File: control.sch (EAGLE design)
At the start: 71 parts, among them IC2 XMEGA16A4A, IC3 LM317MBSTT3, IC5 LM358N, Q1 BSS123, Q2 BSS123, Q3 BC548, Q4 BC557C, Q5 TIP41C, Q6 TIP42C, Q7 BC338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

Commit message: adc angeschlossen
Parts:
- removed JP4, JP6: (no value), jumper:JP4E
- renumbered R17 to R7
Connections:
- new net N$10: R44.2
- new net N$38: R47.2
- new net N$39: R48.2
- new net N$5: R43.2
- net ADC1: now also R45.2
- net ADC2: now also R46.2
- net ADC3: now also R42.2
- net ADC4: now also R41.2, R7.2; no longer R7.1
- net DIS_A: now also IC2.PE3; no longer IC2.PD0
- net EN_A1: now also IC2.PE2; no longer IC2.PD1
- net N$16: now also R7.1; no longer R7.2
- net N$18: no longer JP6.4
- net N$19: no longer JP6.3
- net N$20: no longer JP6.2
- net N$21: no longer JP6.1
- net N$22: no longer JP4.4
- net N$23: no longer JP4.3
- net N$24: no longer JP4.2
- net N$25: no longer JP4.1
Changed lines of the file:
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@@
 <part name="U$3" library="teile" deviceset="STL100NH3LL" device=""/>
 <part name="R16" library="resistor-power" deviceset="R" device="KH208-8R" value="4R7"/>
-<part name="R17" library="resistor-power" deviceset="R" device="KH208-8R" value="4R7"/>
 <part name="IC2" library="atmel" deviceset="XMEGA16A4" device="A"/>
 <part name="C1" library="resistor" deviceset="C-EU" device="C0805K"/>
@@
 <part name="+3V4" library="supply1" deviceset="+3V3" device=""/>
 <part name="P+3" library="supply1" deviceset="+12V" device=""/>
-<part name="JP4" library="jumper" deviceset="JP4E" device=""/>
-<part name="JP6" library="jumper" deviceset="JP4E" device=""/>
 <part name="R13" library="resistor" deviceset="R-EU_" device="M0805"/>
 <part name="R21" library="resistor" deviceset="R-EU_" device="M0805"/>
@@
 <part name="+3V5" library="supply1" deviceset="+3V3" device=""/>
 <part name="GND14" library="supply1" deviceset="GND" device=""/>
+<part name="R7" library="resistor-power" deviceset="R" device="KH208-8R" value="4R7"/>
 </parts>
 <sheets>
@@
 <instance part="U$3" gate="G$1" x="22.86" y="33.02"/>
 <instance part="R16" gate="G$1" x="30.48" y="48.26" rot="R90"/>
-<instance part="R17" gate="G$1" x="30.48" y="73.66" rot="R270"/>
 <instance part="IC2" gate="G$1" x="129.54" y="198.12"/>
 <instance part="C1" gate="G$1" x="91.44" y="210.82"/>
@@
 <instance part="+3V4" gate="G$1" x="60.96" y="266.7"/>
 <instance part="P+3" gate="1" x="25.4" y="266.7"/>
-<instance part="JP4" gate="G$1" x="213.36" y="233.68" rot="R270"/>
-<instance part="JP6" gate="G$1" x="213.36" y="223.52" rot="R270"/>
 <instance part="R13" gate="G$1" x="7.62" y="137.16" rot="R270"/>
 <instance part="R21" gate="G$1" x="45.72" y="119.38" rot="R270"/>
@@
 <instance part="+3V5" gate="G$1" x="71.12" y="233.68"/>
 <instance part="GND14" gate="1" x="76.2" y="233.68"/>
+<instance part="R7" gate="G$1" x="30.48" y="73.66" rot="R90"/>
 </instances>
 <busses>
@@
 <pinref part="IC5" gate="A" pin="-IN"/>
 <wire x1="147.32" y1="60.96" x2="144.78" y2="60.96" width="0.1524" layer="91"/>
+</segment>
+<segment>
+<pinref part="R46" gate="G$1" pin="2"/>
+<wire x1="198.12" y1="256.54" x2="198.12" y2="248.92" width="0.1524" layer="91"/>
+<label x="198.12" y="251.46" size="1.778" layer="95" rot="R90"/>
 </segment>
 </net>
@@
 <junction x="50.8" y="76.2"/>
 </segment>
+<segment>
+<pinref part="R45" gate="G$1" pin="2"/>
+<wire x1="195.58" y1="248.92" x2="195.58" y2="256.54" width="0.1524" layer="91"/>
+<label x="195.58" y="251.46" size="1.778" layer="95" rot="R90"/>
+</segment>
 </net>
 <net name="N$4" class="0">
@@
 <wire x1="96.52" y1="58.42" x2="91.44" y2="58.42" width="0.1524" layer="91"/>
 <junction x="91.44" y="58.42"/>
+</segment>
+<segment>
+<pinref part="R42" gate="G$1" pin="2"/>
+<wire x1="187.96" y1="256.54" x2="187.96" y2="248.92" width="0.1524" layer="91"/>
+<label x="187.96" y="251.46" size="1.778" layer="95" rot="R90"/>
 </segment>
 </net>
@@
 <pinref part="JP5" gate="G$1" pin="2"/>
 <wire x1="25.4" y1="58.42" x2="30.48" y2="58.42" width="0.1524" layer="91"/>
-<pinref part="R17" gate="G$1" pin="2"/>
 <wire x1="30.48" y1="58.42" x2="30.48" y2="68.58" width="0.1524" layer="91"/>
+<pinref part="R7" gate="G$1" pin="1"/>
 </segment>
 </net>
@@
 <wire x1="30.48" y1="81.28" x2="30.48" y2="99.06" width="0.1524" layer="91"/>
 <wire x1="30.48" y1="99.06" x2="45.72" y2="99.06" width="0.1524" layer="91"/>
-<pinref part="R17" gate="G$1" pin="1"/>
 <wire x1="30.48" y1="78.74" x2="30.48" y2="81.28" width="0.1524" layer="91"/>
 <junction x="30.48" y="81.28"/>
@@
 <wire x1="55.88" y1="137.16" x2="55.88" y2="132.08" width="0.1524" layer="91"/>
 <junction x="63.5" y="137.16"/>
+<pinref part="R7" gate="G$1" pin="2"/>
+</segment>
+<segment>
+<pinref part="R41" gate="G$1" pin="2"/>
+<wire x1="185.42" y1="248.92" x2="185.42" y2="256.54" width="0.1524" layer="91"/>
+<label x="185.42" y="251.46" size="1.778" layer="95" rot="R90"/>
 </segment>
 </net>
@@
 <pinref part="IC2" gate="G$1" pin="PA0"/>
 <wire x1="157.48" y1="218.44" x2="185.42" y2="218.44" width="0.1524" layer="91"/>
-<pinref part="JP6" gate="G$1" pin="4"/>
 <pinref part="R33" gate="G$1" pin="2"/>
 <wire x1="185.42" y1="218.44" x2="210.82" y2="218.44" width="0.1524" layer="91"/>
@@
 <pinref part="IC2" gate="G$1" pin="PA1"/>
 <wire x1="157.48" y1="220.98" x2="187.96" y2="220.98" width="0.1524" layer="91"/>
-<pinref part="JP6" gate="G$1" pin="3"/>
 <pinref part="R42" gate="G$1" pin="1"/>
 <pinref part="R34" gate="G$1" pin="2"/>
@@
 <pinref part="IC2" gate="G$1" pin="PA2"/>
 <wire x1="157.48" y1="223.52" x2="190.5" y2="223.52" width="0.1524" layer="91"/>
-<pinref part="JP6" gate="G$1" pin="2"/>
 <pinref part="R35" gate="G$1" pin="2"/>
 <pinref part="R43" gate="G$1" pin="1"/>
@@
 <pinref part="IC2" gate="G$1" pin="PA3"/>
 <wire x1="210.82" y1="226.06" x2="193.04" y2="226.06" width="0.1524" layer="91"/>
-<pinref part="JP6" gate="G$1" pin="1"/>
 <pinref part="R44" gate="G$1" pin="1"/>
 <pinref part="R36" gate="G$1" pin="2"/>
@@
 <pinref part="IC2" gate="G$1" pin="PA4"/>
 <wire x1="157.48" y1="228.6" x2="195.58" y2="228.6" width="0.1524" layer="91"/>
-<pinref part="JP4" gate="G$1" pin="4"/>
 <pinref part="R37" gate="G$1" pin="2"/>
 <pinref part="R45" gate="G$1" pin="1"/>
@@
 <pinref part="IC2" gate="G$1" pin="PA5"/>
 <wire x1="210.82" y1="231.14" x2="198.12" y2="231.14" width="0.1524" layer="91"/>
-<pinref part="JP4" gate="G$1" pin="3"/>
 <pinref part="R46" gate="G$1" pin="1"/>
 <pinref part="R38" gate="G$1" pin="2"/>
@@
 <pinref part="IC2" gate="G$1" pin="PA6"/>
 <wire x1="157.48" y1="233.68" x2="200.66" y2="233.68" width="0.1524" layer="91"/>
-<pinref part="JP4" gate="G$1" pin="2"/>
 <pinref part="R39" gate="G$1" pin="2"/>
 <pinref part="R47" gate="G$1" pin="1"/>
@@
 <pinref part="IC2" gate="G$1" pin="PA7"/>
 <wire x1="210.82" y1="236.22" x2="203.2" y2="236.22" width="0.1524" layer="91"/>
-<pinref part="JP4" gate="G$1" pin="1"/>
 <pinref part="R48" gate="G$1" pin="1"/>
 <pinref part="R40" gate="G$1" pin="2"/>
@@
 </segment>
 <segment>
-<pinref part="IC2" gate="G$1" pin="PD0"/>
-<wire x1="157.48" y1="160.02" x2="162.56" y2="160.02" width="0.1524" layer="91"/>
+<pinref part="IC2" gate="G$1" pin="PE3"/>
+<wire x1="104.14" y1="167.64" x2="96.52" y2="167.64" width="0.1524" layer="91"/>
+<label x="96.52" y="167.64" size="1.778" layer="95"/>
 </segment>
 </net>
@@
 </segment>
 <segment>
-<pinref part="IC2" gate="G$1" pin="PD1"/>
-<wire x1="157.48" y1="162.56" x2="162.56" y2="162.56" width="0.1524" layer="91"/>
+<pinref part="IC2" gate="G$1" pin="PE2"/>
+<wire x1="104.14" y1="165.1" x2="96.52" y2="165.1" width="0.1524" layer="91"/>
+<label x="96.52" y="165.1" size="1.778" layer="95"/>
 </segment>
 </net>
@@
 <pinref part="IC2" gate="G$1" pin="PD2"/>
 <wire x1="157.48" y1="165.1" x2="162.56" y2="165.1" width="0.1524" layer="91"/>
+<label x="160.02" y="165.1" size="1.778" layer="95"/>
 </segment>
 </net>
@@
 </segment>
 </net>
+<net name="N$5" class="0">
+<segment>
+<pinref part="R43" gate="G$1" pin="2"/>
+<wire x1="190.5" y1="248.92" x2="190.5" y2="256.54" width="0.1524" layer="91"/>
+<label x="190.5" y="251.46" size="1.778" layer="95" rot="R90"/>
+</segment>
+</net>
+<net name="N$10" class="0">
+<segment>
+<pinref part="R44" gate="G$1" pin="2"/>
+<wire x1="193.04" y1="256.54" x2="193.04" y2="248.92" width="0.1524" layer="91"/>
+<label x="193.04" y="251.46" size="1.778" layer="95" rot="R90"/>
+</segment>
+</net>
+<net name="N$38" class="0">
+<segment>
+<pinref part="R47" gate="G$1" pin="2"/>
+<wire x1="200.66" y1="248.92" x2="200.66" y2="256.54" width="0.1524" layer="91"/>
+<label x="200.66" y="251.46" size="1.778" layer="95" rot="R90"/>
+</segment>
+</net>
+<net name="N$39" class="0">
+<segment>
+<pinref part="R48" gate="G$1" pin="2"/>
+<wire x1="203.2" y1="256.54" x2="203.2" y2="248.92" width="0.1524" layer="91"/>
+<label x="203.2" y="251.46" size="1.778" layer="95" rot="R90"/>
+</segment>
+</net>

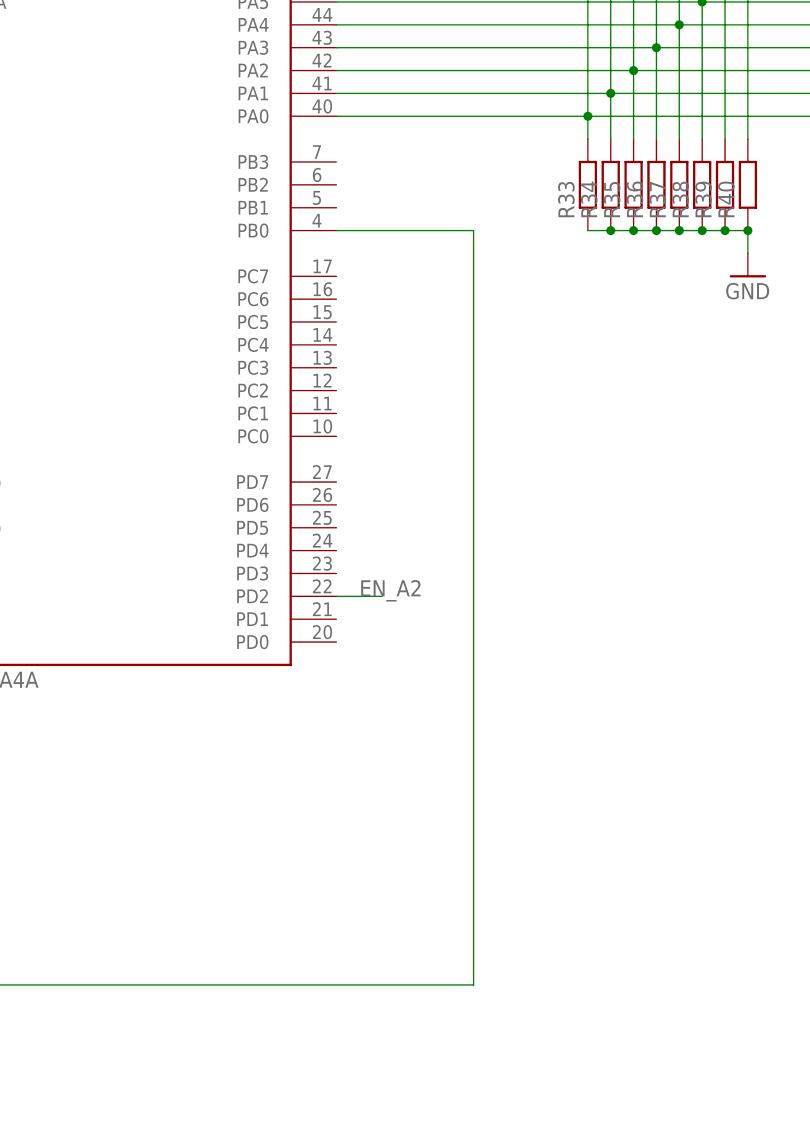
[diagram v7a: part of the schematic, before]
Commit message: DAC pin corrected
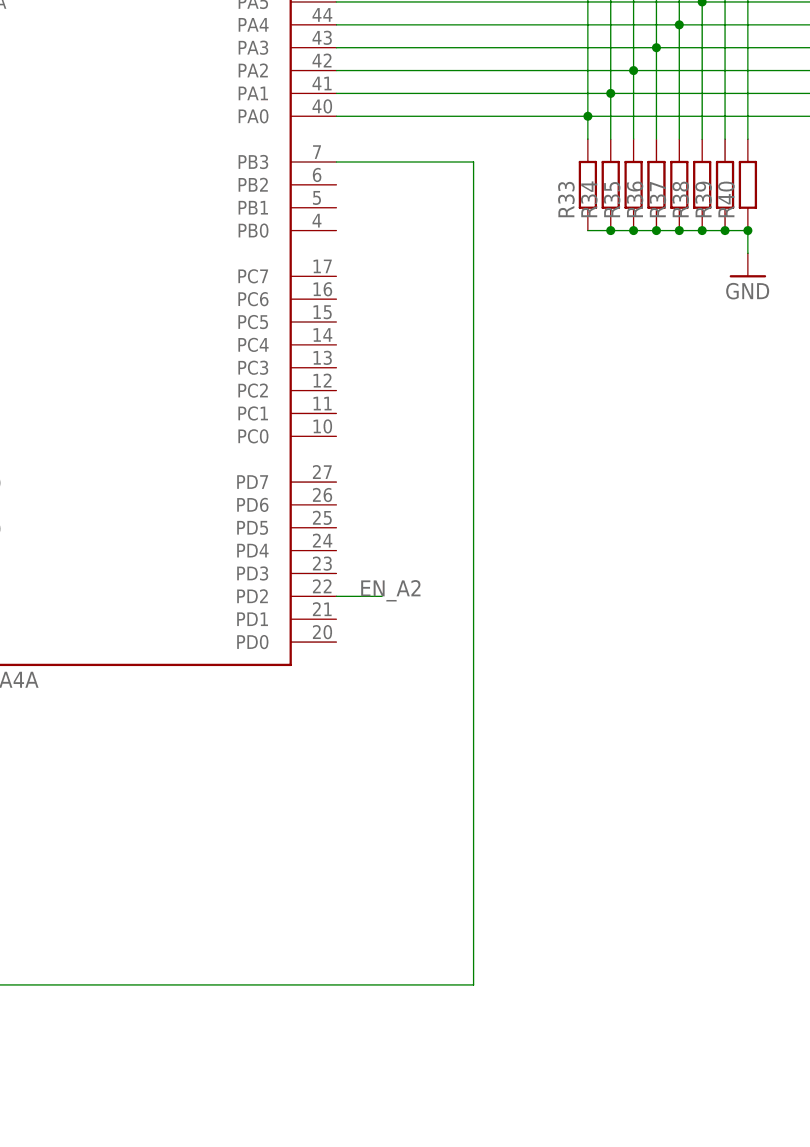
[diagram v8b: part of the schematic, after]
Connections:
- net N$31: now also IC2.PB3; no longer IC2.PB0
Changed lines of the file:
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@@
 <net name="N$31" class="0">
 <segment>
-<pinref part="IC2" gate="G$1" pin="PB0"/>
-<wire x1="157.48" y1="205.74" x2="172.72" y2="205.74" width="0.1524" layer="91"/>
-<wire x1="172.72" y1="205.74" x2="172.72" y2="121.92" width="0.1524" layer="91"/>
+<wire x1="172.72" y1="213.36" x2="172.72" y2="121.92" width="0.1524" layer="91"/>
 <wire x1="172.72" y1="121.92" x2="33.02" y2="121.92" width="0.1524" layer="91"/>
 <wire x1="33.02" y1="121.92" x2="33.02" y2="119.38" width="0.1524" layer="91"/>
 <pinref part="IC5" gate="B" pin="+IN"/>
+<wire x1="172.72" y1="213.36" x2="157.48" y2="213.36" width="0.1524" layer="91"/>
+<pinref part="IC2" gate="G$1" pin="PB3"/>
 </segment>
 </net>
